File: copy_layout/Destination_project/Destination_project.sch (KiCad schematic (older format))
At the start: 1 part, among them U1 LAUNCHXL-F28379D

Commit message: Delna verzija
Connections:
- net power/Ql: now reaches U1.37 (GPIO3/EPWM2B)
- net power/QH: now reaches U1.38 (GPIO2/EPWM2A)
- net Leg1/HIN renamed Leg/QH
- net Leg1/LIN renamed Leg/QL
- net Leg1/TOK renamed Leg/Current
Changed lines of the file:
@@
 $Descr A4 11693 8268
 encoding utf-8
-Sheet 1 2
+Sheet 1 6
 Title ""
 Date ""
@@
 Wire Wire Line
 	4100 6400 4200 6400
-$Sheet
-S 7000 2400 1000 1000
-U 5CA367A0
-F0 "Leg1" 50
-F1 "Leg.sch" 50
-F2 "HIN" I L 7000 2800 50
-F3 "LIN" I L 7000 2900 50
-F4 "TOK" O R 8000 2900 50
-$EndSheet
 Wire Wire Line
 	7000 2800 5700 2800
@@
 Wire Wire Line
 	2700 3000 3100 3000
+$Sheet
+S 7000 3650 1000 1000
+U 5CADA2A6
+F0 "power" 50
+F1 "Power.sch" 50
+F2 "OUT" O R 8000 4050 50
+F3 "QH" I L 7000 3950 50
+F4 "Ql" I L 7000 4150 50
+$EndSheet
+$Sheet
+S 7000 2450 1000 1000
+U 5CADA6B4
+F0 "Leg" 50
+F1 "Leg.sch" 50
+F2 "QH" I L 7000 2800 50
+F3 "QL" I L 7000 2900 50
+F4 "Current" O R 8000 2900 50
+$EndSheet
+Wire Wire Line
+	7000 3950 6750 3950
+Wire Wire Line
+	6750 3950 6750 3000
+Wire Wire Line
+	6750 3000 5700 3000
+Wire Wire Line
+	7000 4150 6650 4150
+Wire Wire Line
+	6650 4150 6650 3100
+Wire Wire Line
+	6650 3100 5700 3100
 $EndSCHEMATC

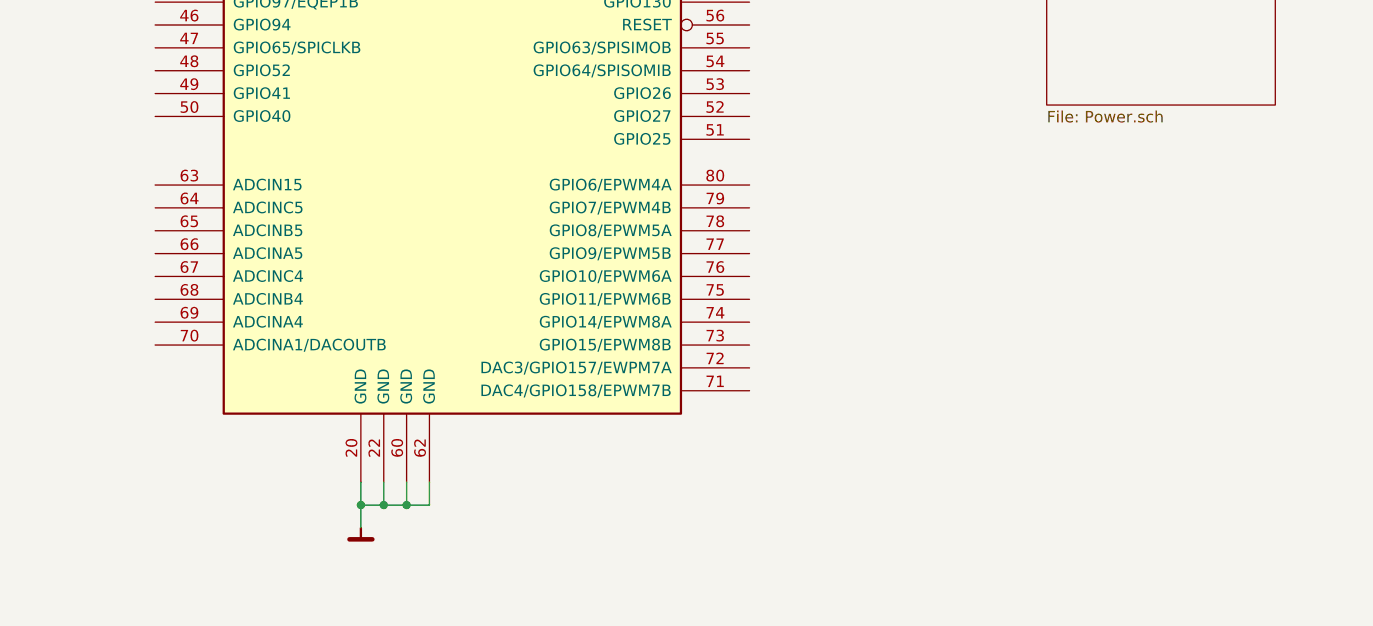
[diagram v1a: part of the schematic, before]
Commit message: Modified test project. Successfule began importing layout
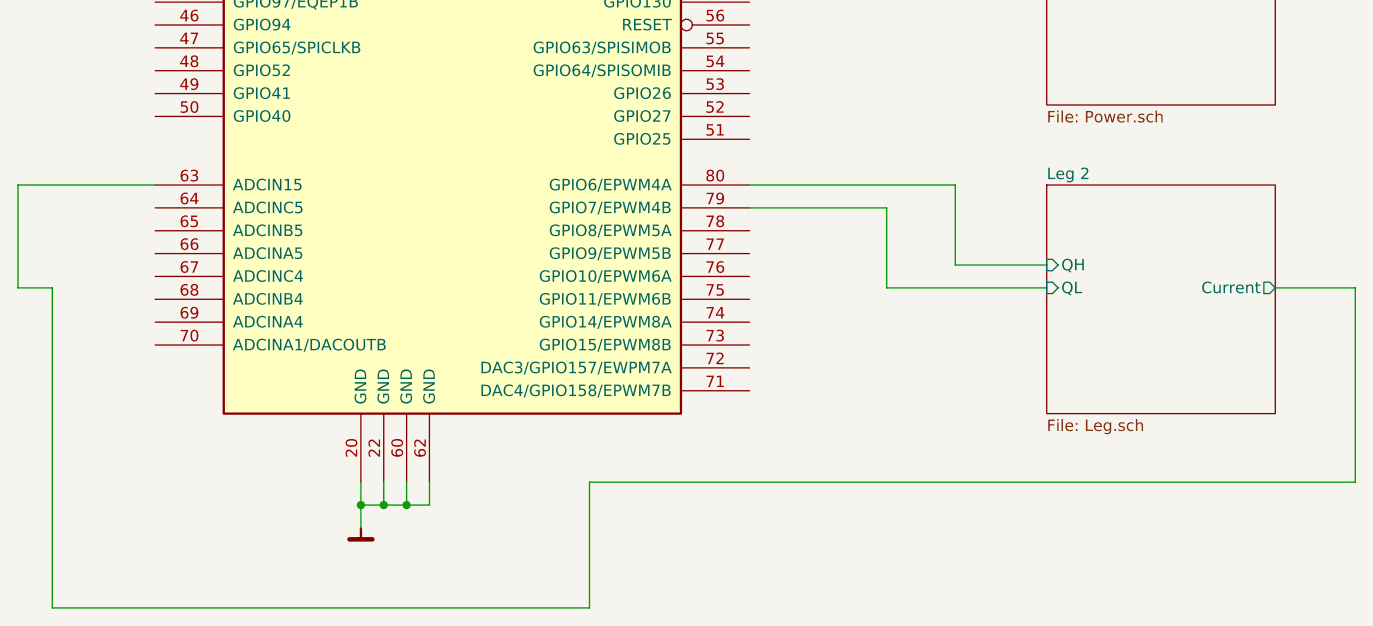
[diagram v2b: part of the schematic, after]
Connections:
- net Leg 2/Current: now reaches U1.63 (ADCIN15)
- net Leg 2/QL: now reaches U1.79 (GPIO7/EPWM4B)
- net Leg 2/QH: now reaches U1.80 (GPIO6/EPWM4A)
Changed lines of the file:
@@
 $Descr A4 11693 8268
 encoding utf-8
-Sheet 1 6
+Sheet 1 10
 Title ""
 Date ""
@@
 Wire Wire Line
 	6650 3100 5700 3100
+$Sheet
+S 7000 5000 1000 1000
+U 5CAF0FB9
+F0 "Leg 2" 50
+F1 "Leg.sch" 50
+F2 "QH" I L 7000 5350 50
+F3 "QL" I L 7000 5450 50
+F4 "Current" O R 8000 5450 50
+$EndSheet
+Wire Wire Line
+	7000 5350 6600 5350
+Wire Wire Line
+	6600 5350 6600 5000
+Wire Wire Line
+	6600 5000 5700 5000
+Wire Wire Line
+	5700 5100 6300 5100
+Wire Wire Line
+	6300 5100 6300 5450
+Wire Wire Line
+	6300 5450 7000 5450
+Wire Wire Line
+	5000 6300 5000 6850
+Wire Wire Line
+	5000 6850 2650 6850
+Wire Wire Line
+	2650 6850 2650 5450
+Wire Wire Line
+	2650 5450 2500 5450
+Wire Wire Line
+	2500 5450 2500 5000
+Wire Wire Line
+	2500 5000 3100 5000
+Wire Wire Line
+	8350 5450 8350 6300
+Wire Wire Line
+	5000 6300 8350 6300
+Wire Wire Line
+	8000 5450 8350 5450
 $EndSCHEMATC
